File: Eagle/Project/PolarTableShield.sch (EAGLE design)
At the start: 44 parts, among them IC2 LM358D, J1 Pi Power Jack, J10 LED + Radio, J2 Header - Right angled, female, J3 Pi Connection, J4 extra points, J5 IR Sensors, J6 Switch A + B, J7 Switch C + D, J8 Switch E + F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

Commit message: Expanded board
Remove my self imposed footprint restriction.
Add circuit for analog to 1bit digital signal for the IR sensors.
Added the new SX1509 custom device.
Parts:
- removed JP5: Left Sub-board Mount, keir_library:CONN_111X11_2.54MM_FEMALE
- removed JP6: Right Sub-board Mount, keir_library:CONN_111X11_2.54MM_FEMALE
- removed JP7: Top Sub-board Mount, keir_library:CONN_071X07_2.54MM_FEMALE
- added JP1: (no value), pinhead:PINHD-1X4
- added U$1: SX1509, keir_library:SX1509
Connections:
- removed net B0: J10.1, JP5.4
- removed net B10: J6.3, JP6.9
- removed net B11: J6.4, JP6.8
- removed net B12: J9G$1.O, JP6.7, R12.1, U1G1.OUT
- removed net B13: J9G$2.O, JP6.6, R6.1, U1G2.OUT
- removed net B14: J9G$3.O, JP6.5, R11.1, U1G3.OUT
- removed net B15: J9G$4.O, JP6.4, R10.1, U1G4.OUT
- removed net B5: J8.3, JP5.9
- removed net B6: J8.4, JP5.10
- removed net B8: J7.3, JP6.11
- removed net B9: J7.4, JP6.10
- removed net NINT: B1.D2, JP7.6
- removed net RES: B1.RES, B2.RES, JP7.2, Q3.E
- new net !INT: B1.D2, U$1G$1.!RST
- new net !RES: B1.RES, B2.RES, Q3.E, U$1G$1.!INT
- new net B1: U$1G$2.P$1
- new net B2: U$1G$2.P$2
- new net B3: U$1G$2.P$3
- new net IR_G: J9G$1.O, R12.1, U$1G$3.P$15, U1G1.OUT
- new net IR_H: J9G$2.O, R6.1, U$1G$3.P$14, U1G2.OUT
- new net IR_I: J9G$3.O, R11.1, U$1G$3.P$13, U1G3.OUT
- new net IR_J: J9G$4.O, R10.1, U$1G$3.P$12, U1G4.OUT
- new net N$18: B1.A2, JP1.3
- new net N$19: B1.A1, JP1.2
- new net N$20: B1.A0, JP1.1
- new net N$6: B1.A3, JP1.4
- new net SW_A: J6.3, U$1G$3.P$11
- new net SW_B: J6.4, U$1G$3.P$10
- new net SW_C: J7.3, U$1G$3.P$9
- new net SW_D: J7.4, U$1G$3.P$8
- new net SW_E: J8.3, U$1G$2.P$6
- new net SW_F: J8.4, U$1G$2.P$7
- new net WAKE_LED: J10.1, U$1G$2.P$5
- net 3.3V: now also U$1G$1.3.3V, U$1G$2.3.3V, U$1G$3.3.3V; no longer JP5.2, JP6.2, JP7.7
- net B4: now also U$1G$2.P$4; no longer JP5.8
- net B7: now also U$1G$2.P$0; no longer J4.3, JP5.11
- net GND: now also U$1G$1.GND, U$1G$2.GND, U$1G$3.GND; no longer JP5.1, JP6.1, JP7.1
- net SCL: now also U$1G$1.SCL; no longer JP7.4
- net SDA: now also U$1G$1.OSCIO; no longer JP7.3
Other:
- note added: "Analog to HIGH/LOW"

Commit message: Back to normal shield size
Removed the sensor analog to digital section.
Added more specific net classes to be explicit about the logic voltage levels of the different boards.
Added 3.3V to 5V logic conversion for the I2C bus.
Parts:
- removed J4: extra points, keir_library:CONN_041X04_1.24MM_RA_MALE
- removed J9: (no value), keir_library:CONN_04X3
- removed JP1: (no value), pinhead:PINHD-1X4
- removed JP4: Route 15 to external, SparkFun-Jumpers:JUMPER-SMT_3_1-NC_TRACE_SILK
- removed U1: LM339PWR, SparkFun-IC-Amplifiers:LM339
- removed VR2: 10k, SparkFun-Resistors:TRIMPOT-PTH-10MM-KNOB-1/2W-10%
- added JP5, JP6: JUMPER-SMT_2_NC_TRACE_NO-SILK, SparkFun-Jumpers:JUMPER-SMT_2_NC_TRACE_NO-SILK
- added Q4, Q5: 2N7000, keir_library:2N7000
- JP2: device SparkFun-Jumpers:JUMPER-SMT_2_NO_SILK_ROUND -> SparkFun-Jumpers:JUMPER-SMT_2_NO_SILK
- R10, R11, R12, R6: value 221k -> 4.7k
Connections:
- net 12V renamed 12V_SUPPLY
- net PI_5V renamed 5V_SUPPLY
- removed net 15_PLUG: J4.2, JP4.1
- removed net N$10: J9G$2.S, U1G2.-IN
- removed net N$11: J5.4, J9G$3.P
- removed net N$12: J9G$4.S, U1G4.-IN
- removed net N$13: J9G$3.S, U1G3.-IN
- removed net N$14: J9G$1.S, U1G1.-IN
- removed net N$15: J5.5, J9G$2.P
- removed net N$16: J5.3, J9G$4.P
- removed net N$17: R10.2, R11.2, R12.2, R6.2, U1G1.+IN, U1G2.+IN, U1G3.+IN, U1G4.+IN, VR2.WIPER
- removed net N$18: B1.A2, JP1.3
- removed net N$19: B1.A1, JP1.2
- removed net N$20: B1.A0, JP1.1
- removed net N$9: J5.6, J9G$1.P
- new net A0: B1.A0
- new net A1: B1.A1
- new net A2: B1.A2
- new net SCL_3V: J3.3, Q5.S, R11.2, U$1G$1.SCL
- new net SCL_5V: JP6.1, Q5.D, R10.2
- new net SDA_3V: J3.4, Q4.S, R12.2, U$1G$1.OSCIO
- new net SDA_5V: JP5.1, Q4.D, R6.2
- net !RES: no longer U$1G$1.!INT
- net 3.3V: now also Q4.G, Q5.G, R11.1, R12.1; no longer IC2P.V+, J4.1, Q2.E, R4.2, R8.1, R9.1, U$1G$2.3.3V, U$1G$3.3.3V, U1G5.P$V+, U3.!SRCLR, U3.VCC, VR2.CCW
- net 5V: now also IC2P.V+, Q2.E, R10.1, R4.2, R6.1, R8.1, R9.1, U3.!SRCLR, U3.VCC
- net B4: no longer JP4.2
- net GND: no longer C1.-, C9.2, J1.GND, J1.GNDBREAK, J2.2, J4.4, U$1G$2.GND, U$1G$3.GND, U1G5.P$V-, VR2.CW
- net IR_G: now also J5.6; no longer J9G$1.O, R12.1, U1G1.OUT
- net IR_H: now also J5.5; no longer J9G$2.O, R6.1, U1G2.OUT
- net IR_I: now also J5.4; no longer J9G$3.O, R11.1, U1G3.OUT
- net IR_J: now also J5.3; no longer J9G$4.O, R10.1, U1G4.OUT
- net N$6: now also C1.-, C9.2, J1.GND, J1.GNDBREAK, J2.2; no longer B1.A3, JP1.4
- net PIPOWER_SIGNAL: now also B1.A3; no longer JP4.3
- net SCL: now also JP6.2; no longer J3.3, U$1G$1.SCL
- net SDA: now also JP5.2; no longer J3.4, U$1G$1.OSCIO
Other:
- note removed: "Analog to HIGH/LOW"
- moved on the sheet: R10, R11, R12, R6

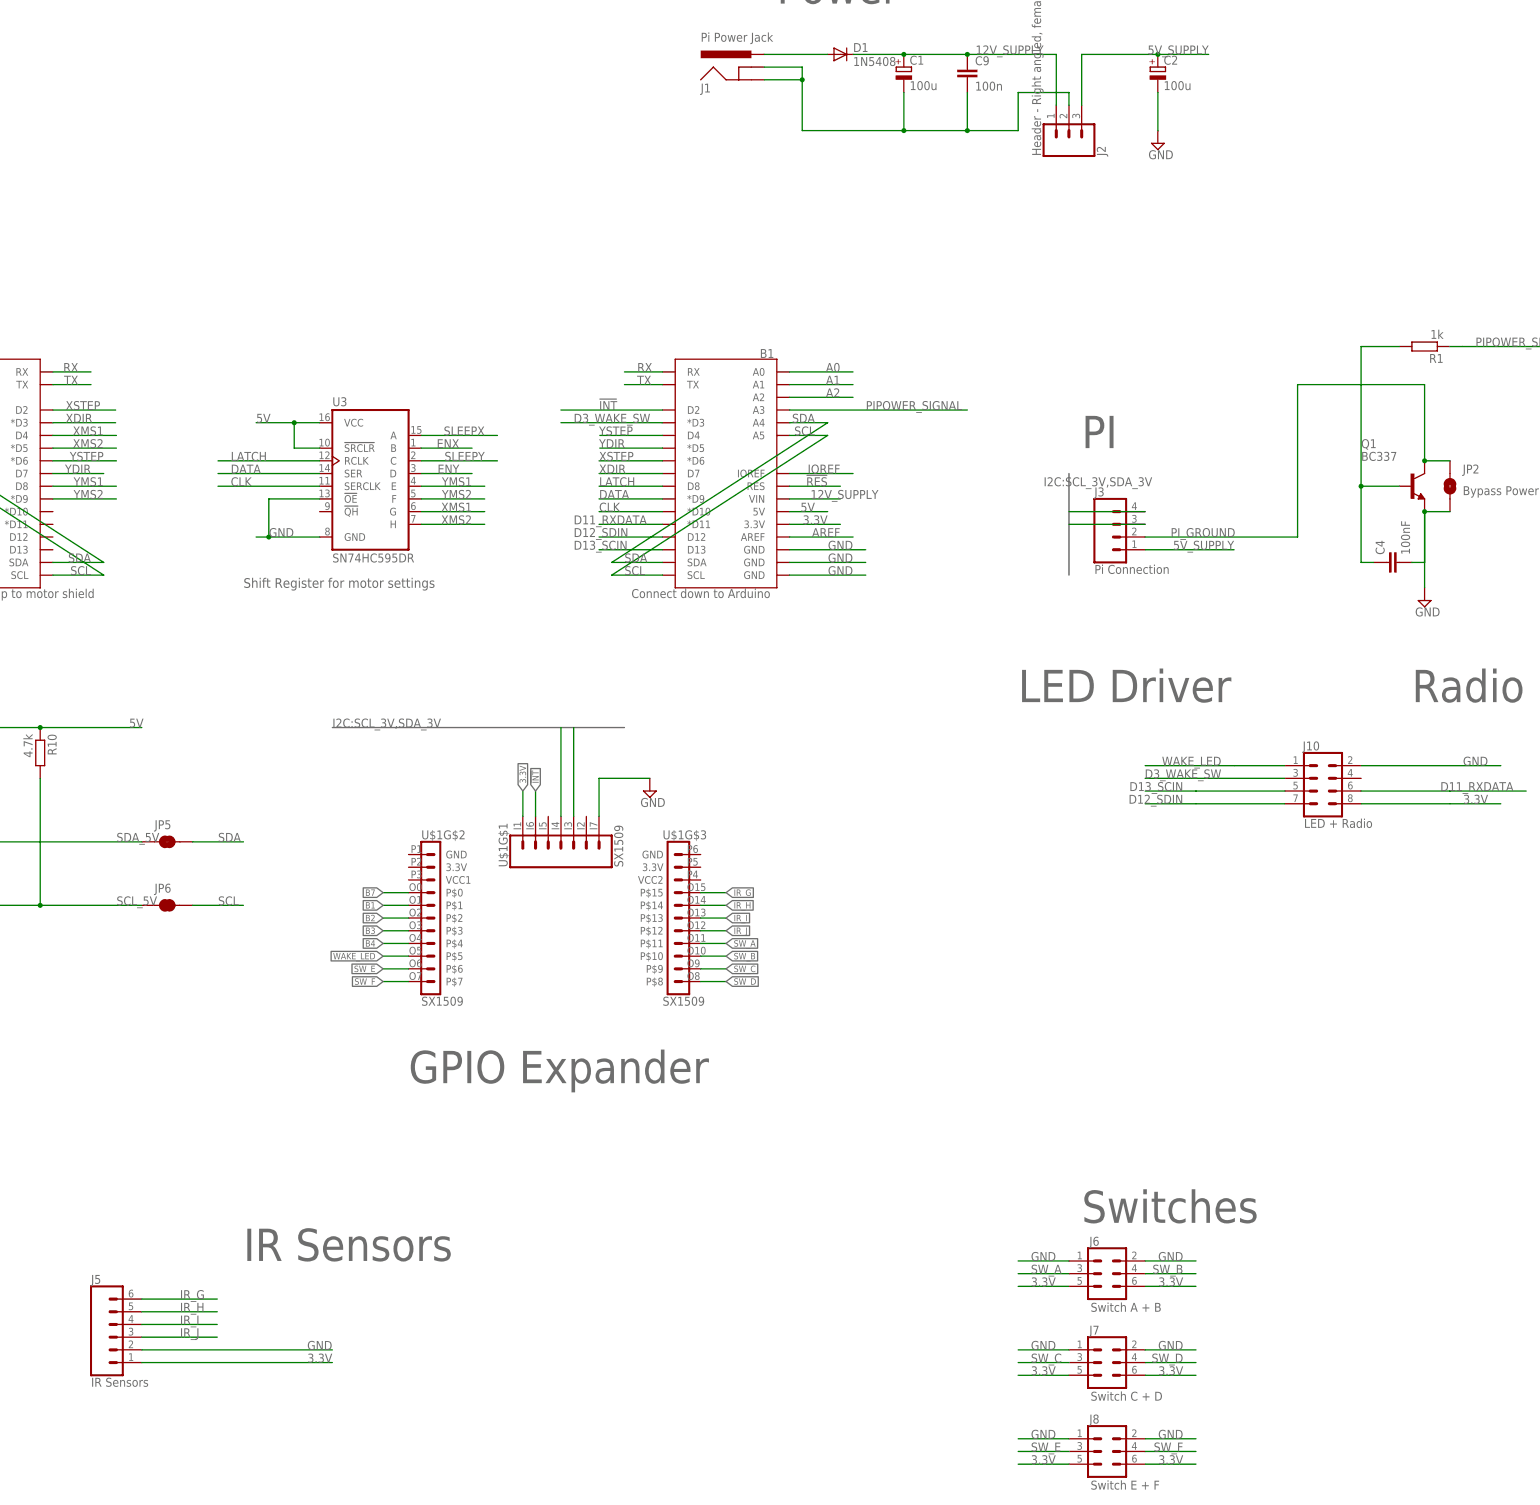
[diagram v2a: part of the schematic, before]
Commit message: Layed out existing design. Added headers for all pins.
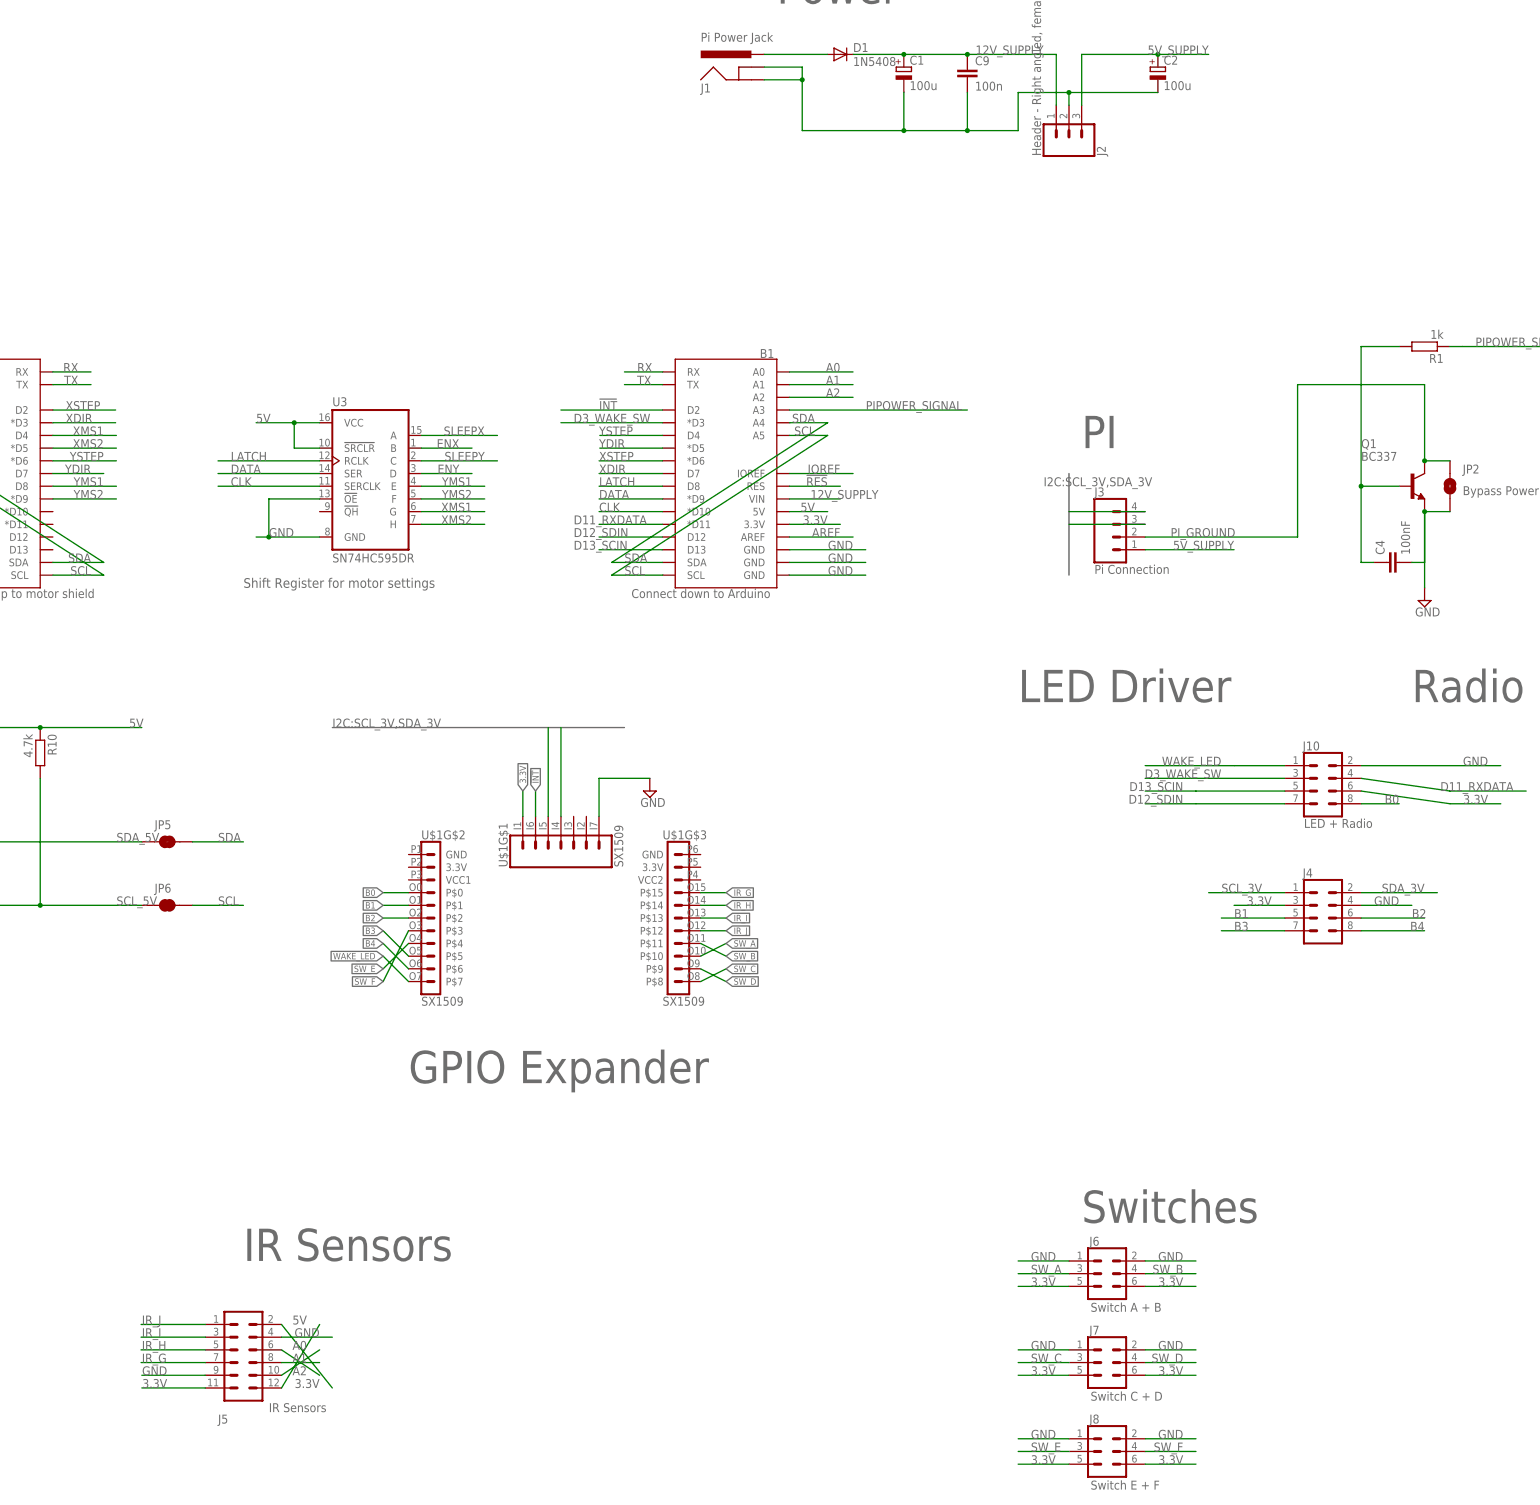
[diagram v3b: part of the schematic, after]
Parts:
- added J4: (no value), keir_library:CONN_04X22X4_1.24MM_RA_MALE
- J5: device SparkFun-Connectors:CONN_06SILK_FEMALE_PTH -> keir_library:CONN_06X21.24MM_RA_MALE
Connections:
- removed net B7: U$1G$2.P$0
- new net B0: J10.8, U$1G$2.P$0
- net 3.3V: now also J10.6, J4.3, J5.11, J5.2; no longer J10.8, J5.1
- net 5V: now also J5.12
- net A0: now also J5.10
- net A1: now also J5.8
- net A2: now also J5.6
- net B1: now also J4.5
- net B2: now also J4.6
- net B3: now also J4.7, U$1G$2.P$5; no longer U$1G$2.P$3
- net B4: now also J4.8, U$1G$2.P$6; no longer U$1G$2.P$4
- net D11_RXDATA: now also J10.4; no longer J10.6
- net GND: now also J4.4, J5.4, J5.9; no longer C2.-, J5.2
- net IR_G: now also J5.7; no longer J5.6
- net IR_I: now also J5.3; no longer J5.4
- net IR_J: now also J5.1; no longer J5.3
- net N$6: now also C2.-
- net SCL_3V: now also J4.1
- net SDA_3V: now also J4.2, U$1G$1.SDA; no longer U$1G$1.OSCIO
- net SW_A: now also U$1G$3.P$10; no longer U$1G$3.P$11
- net SW_B: now also U$1G$3.P$11; no longer U$1G$3.P$10
- net SW_C: now also U$1G$3.P$8; no longer U$1G$3.P$9
- net SW_D: now also U$1G$3.P$9; no longer U$1G$3.P$8
- net SW_E: now also U$1G$2.P$4; no longer U$1G$2.P$6
- net SW_F: now also U$1G$2.P$3; no longer U$1G$2.P$7
- net WAKE_LED: now also U$1G$2.P$7; no longer U$1G$2.P$5
